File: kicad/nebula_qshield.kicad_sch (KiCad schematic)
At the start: 0 parts

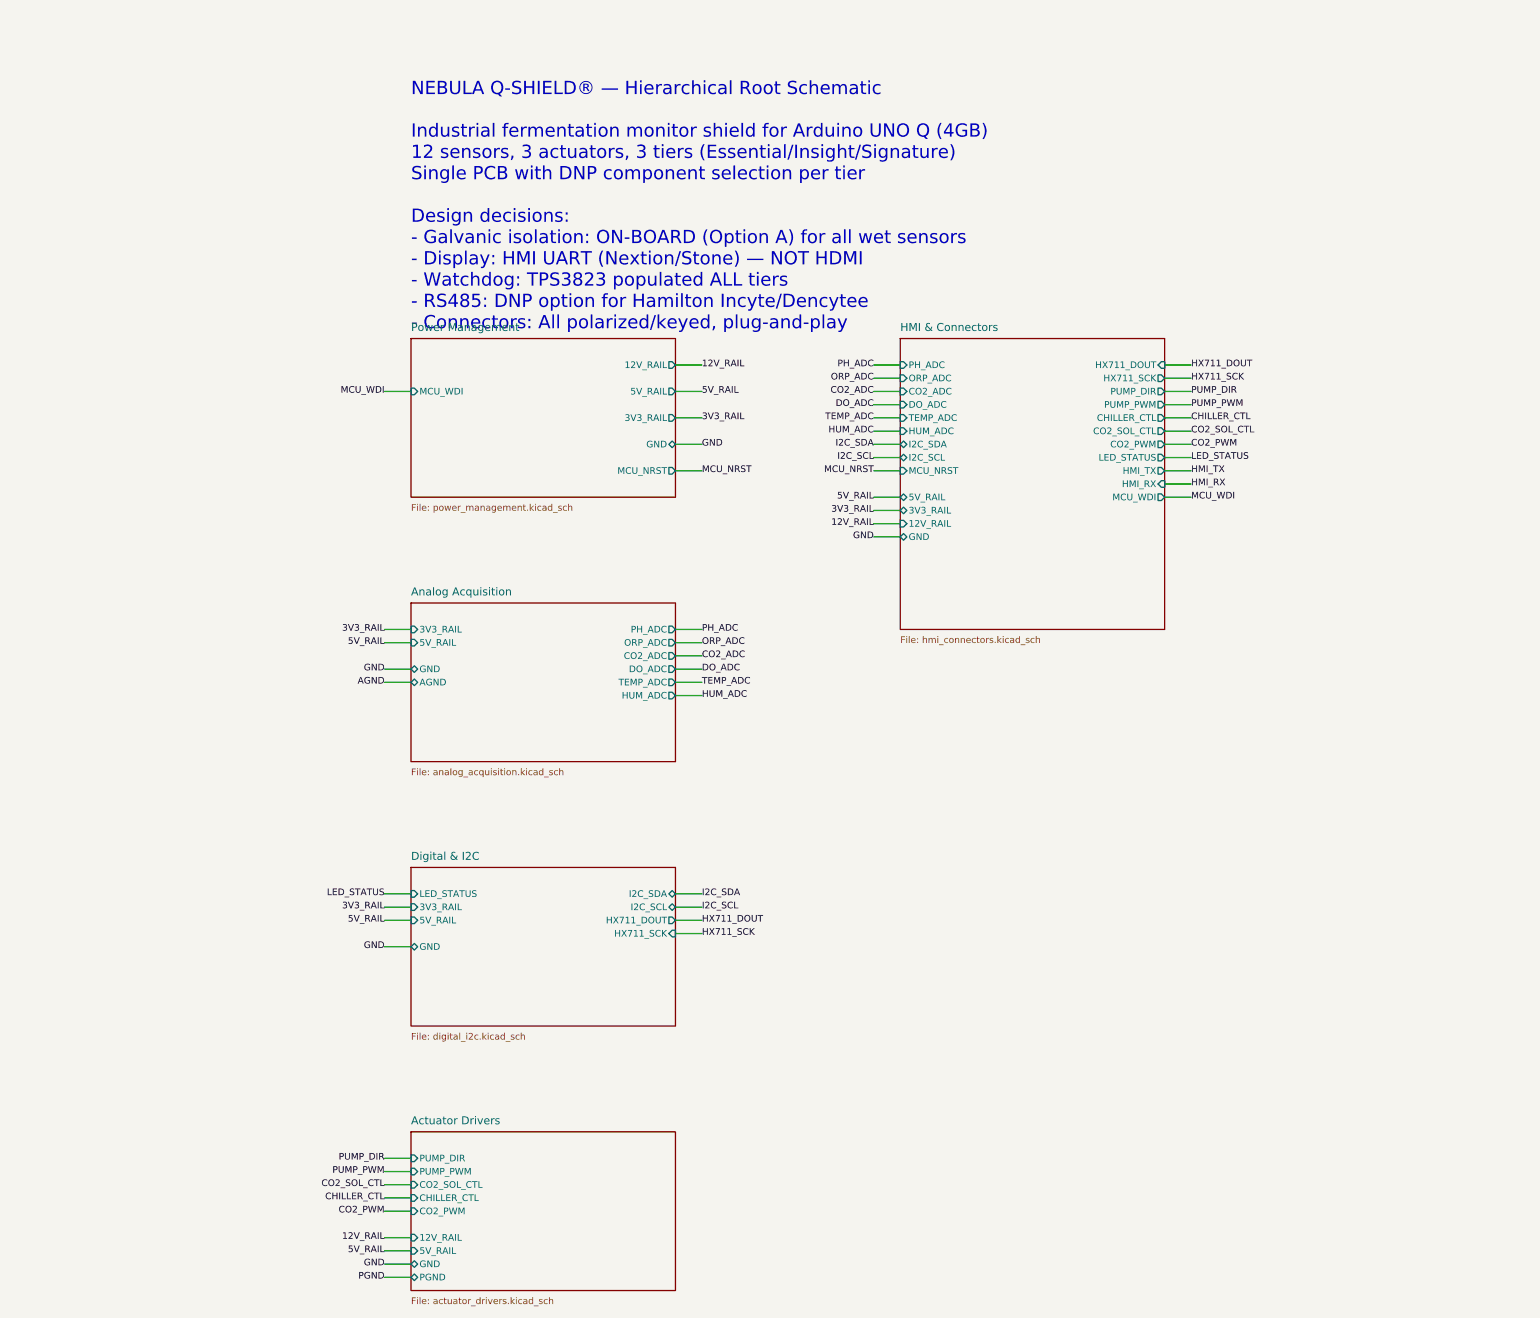
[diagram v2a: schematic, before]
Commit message: fix(grounding): unify AGND/PGND into GND, migrate CI to KiCad 10.0.5 — ERC 14→0
AGND and PGND were fully isolated nets with no path to GND, so the actuator
return path (MOSFET sources, opto emitters, gate-driver COM, flyback diodes,
terminal blocks) and the CO2/humidity sensor returns were floating. Merge them
into the single global GND net per the unified-grounding decision: one
continuous plane on layer 2, star grounding realised through placement and
local vias rather than split nets.

The isolated domains are untouched — GND_ISO_PH/ORP/DO (AMC1301 + SN6501
transformer) and GND_ISO (ISO1541) stay floating, since the galvanic barrier
lives in the isolators, not in a second ground plane.

- analog_acquisition: 2 AGND labels -> GND, legend stub removed
- actuator_drivers: 12 PGND labels -> GND, legend stub and its now-redundant
  PWR_FLAG removed
- hmi_connectors: HMI_TX/HMI_RX demoted from hierarchical to local labels; the
  UART is fully routed inside the sheet and nothing consumed the export
- root: 4 orphan sheet pins with their stub wires and labels removed
- CI container 9.0 -> 10.0.5, ERC severities pinned in the project file so the
  gate cannot weaken through a version bump, threshold 14 -> 0

Netlist verified pin-by-pin: 495 pins before and after, none lost or added,
exactly the 20 intended net reassignments. ERC clean under KiCad 10.0.5.

Co-Authored-By: Devin AI <158243242+devin-ai-integration[bot]@users.noreply.github.com>
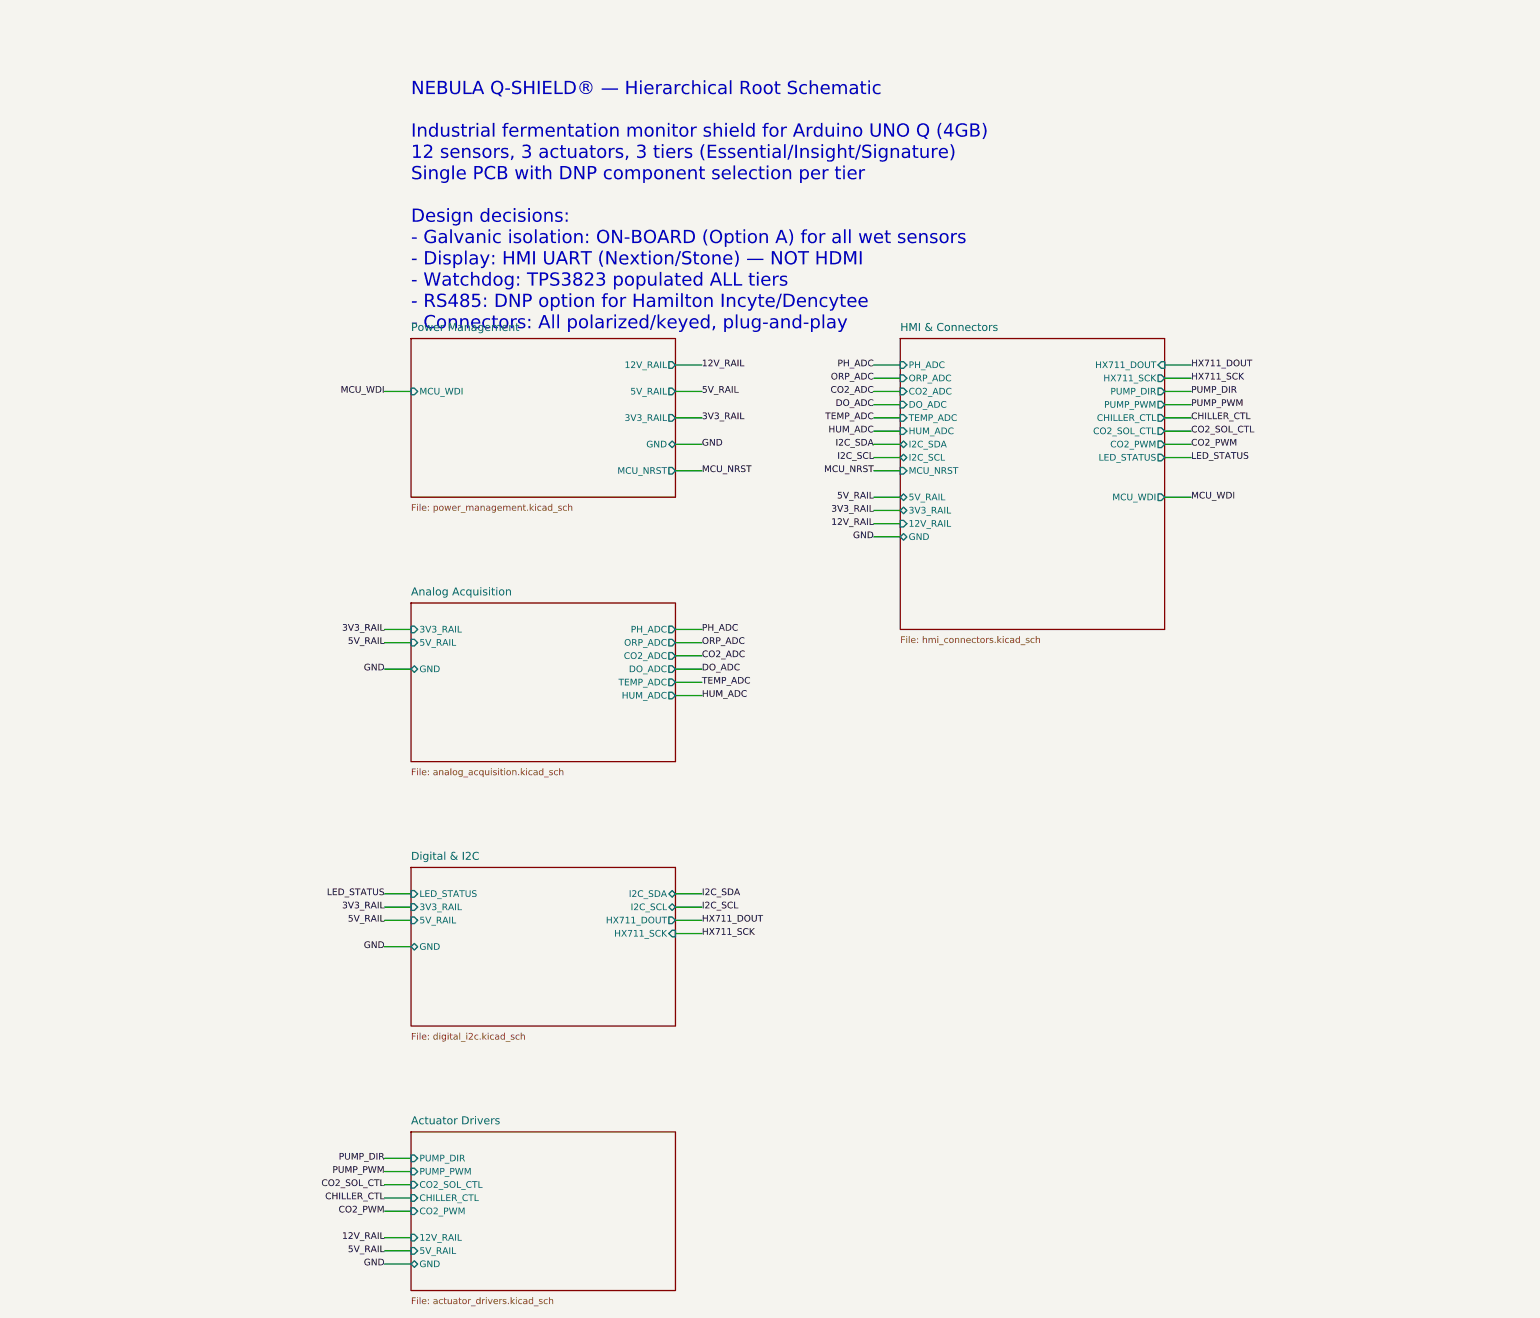
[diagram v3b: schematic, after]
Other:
- sheet Actuator Drivers ports: added none; removed PGND
- sheet Analog Acquisition ports: added none; removed AGND
- sheet HMI & Connectors ports: added none; removed HMI_RX, HMI_TX
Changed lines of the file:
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@@
     (pin "5V_RAIL"   input       (at 25.4 109.22 180)(effects (font (size 1.27 1.27))))
     (pin "GND"       bidirectional (at 25.4 114.3 180)(effects (font (size 1.27 1.27))))
-    (pin "AGND"      bidirectional (at 25.4 116.84 180)(effects (font (size 1.27 1.27))))
   )
   (sheet
@@
     (pin "5V_RAIL"     input   (at 25.4 226.06 180)  (effects (font (size 1.27 1.27))))
     (pin "GND"         bidirectional (at 25.4 228.6 180)(effects (font (size 1.27 1.27))))
-    (pin "PGND"        bidirectional (at 25.4 231.14 180)(effects (font (size 1.27 1.27))))
   )
   (sheet
@@
     (pin "CO2_PWM"     output      (at 170.18 71.12 0)    (effects (font (size 1.27 1.27))))
     (pin "LED_STATUS"  output      (at 170.18 73.66 0)    (effects (font (size 1.27 1.27))))
-    (pin "HMI_TX"      output      (at 170.18 76.2 0)     (effects (font (size 1.27 1.27))))
-    (pin "HMI_RX"      input       (at 170.18 78.74 0)    (effects (font (size 1.27 1.27))))
     (pin "MCU_WDI"     output      (at 170.18 81.28 0)    (effects (font (size 1.27 1.27))))
     (pin "MCU_NRST"    input       (at 119.38 76.2 180)   (effects (font (size 1.27 1.27))))
@@
   (wire (pts (xy 119.38 88.90) (xy 114.30 88.90)) (stroke (width 0) (type default)))
   (label "GND" (at 114.30 88.90 180) (effects (font (size 1.27 1.27))))
-  (wire (pts (xy 25.40 231.14) (xy 20.32 231.14)) (stroke (width 0) (type default)))
-  (label "PGND" (at 20.32 231.14 180) (effects (font (size 1.27 1.27))))
-  (wire (pts (xy 25.40 116.84) (xy 20.32 116.84)) (stroke (width 0) (type default)))
-  (label "AGND" (at 20.32 116.84 180) (effects (font (size 1.27 1.27))))
   (wire (pts (xy 76.20 106.68) (xy 81.28 106.68)) (stroke (width 0) (type default)))
   (label "PH_ADC" (at 81.28 106.68 0) (effects (font (size 1.27 1.27))))
@@
   (wire (pts (xy 119.38 76.20) (xy 114.30 76.20)) (stroke (width 0) (type default)))
   (label "MCU_NRST" (at 114.30 76.20 180) (effects (font (size 1.27 1.27))))
-  (wire (pts (xy 170.18 76.20) (xy 175.26 76.20)) (stroke (width 0) (type default)))
-  (label "HMI_TX" (at 175.26 76.20 0) (effects (font (size 1.27 1.27))))
-  (wire (pts (xy 170.18 78.74) (xy 175.26 78.74)) (stroke (width 0) (type default)))
-  (label "HMI_RX" (at 175.26 78.74 0) (effects (font (size 1.27 1.27))))
 )

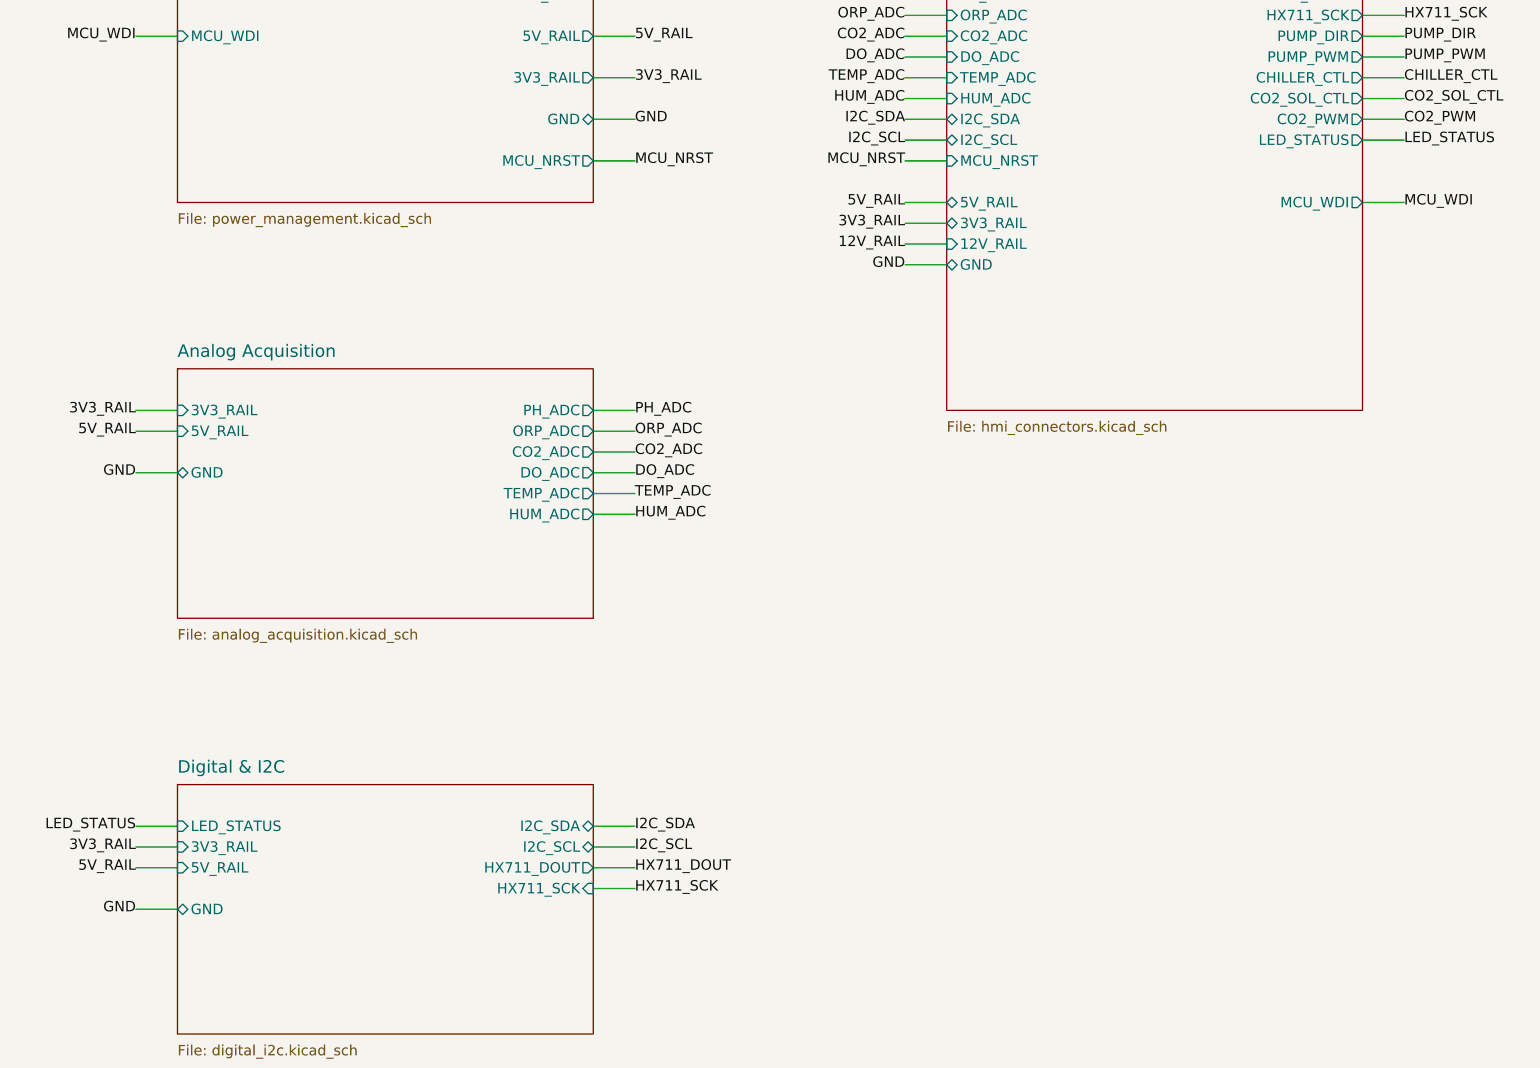
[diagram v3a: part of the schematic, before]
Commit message: feat(rs485): SC16IS740 I2C-UART bridge + realign J21 pin map to firmware
RS485 Modbus had no digital interface: U15's RO/~RE/DE/DI were carrying
no-connect flags, so ERC stayed silent while the transceiver was unusable.
The UNO Q has no free UART TX/RX pair (USART1 is the HMI, the alternate
pairs land on analog pins), so Modbus now hangs off the I2C bus through an
SC16IS740 bridge and coexists with the HMI.

- U22 SC16IS740 on I2C at 0x4D (A0/A1 low), Y1 1.8432 MHz + C31/C32,
  C33 decoupling, R38 pull-up on the open-drain ~IRQ, exported to J21 D10
- U23 SN74LVC1G04 inverts ~RTS into DE/~RE. The bridge leaves ~RTS high
  after POR, which would enable the driver and seize the multidrop bus
  before firmware runs; inverted it resets to driver-off/receive-on
- U15 MAX485ESA -> MAX3485CSA+ (same SOIC-8 pinout) because the bridge is
  not 5 V tolerant; digital_i2c no longer needs the 5 V rail
- J21 realigned to the firmware: D4=MCU_WDI, D6=PUMP_DIR, D8=CHILLER_CTL,
  D9=CO2_PWM. WDI previously shared D8 with the chiller relay, so driving
  the chiller would have kicked the watchdog

ERC 0 under KiCad 10.0.5; netlist diff limited to the intended pins.

Co-Authored-By: Devin AI <158243242+devin-ai-integration[bot]@users.noreply.github.com>
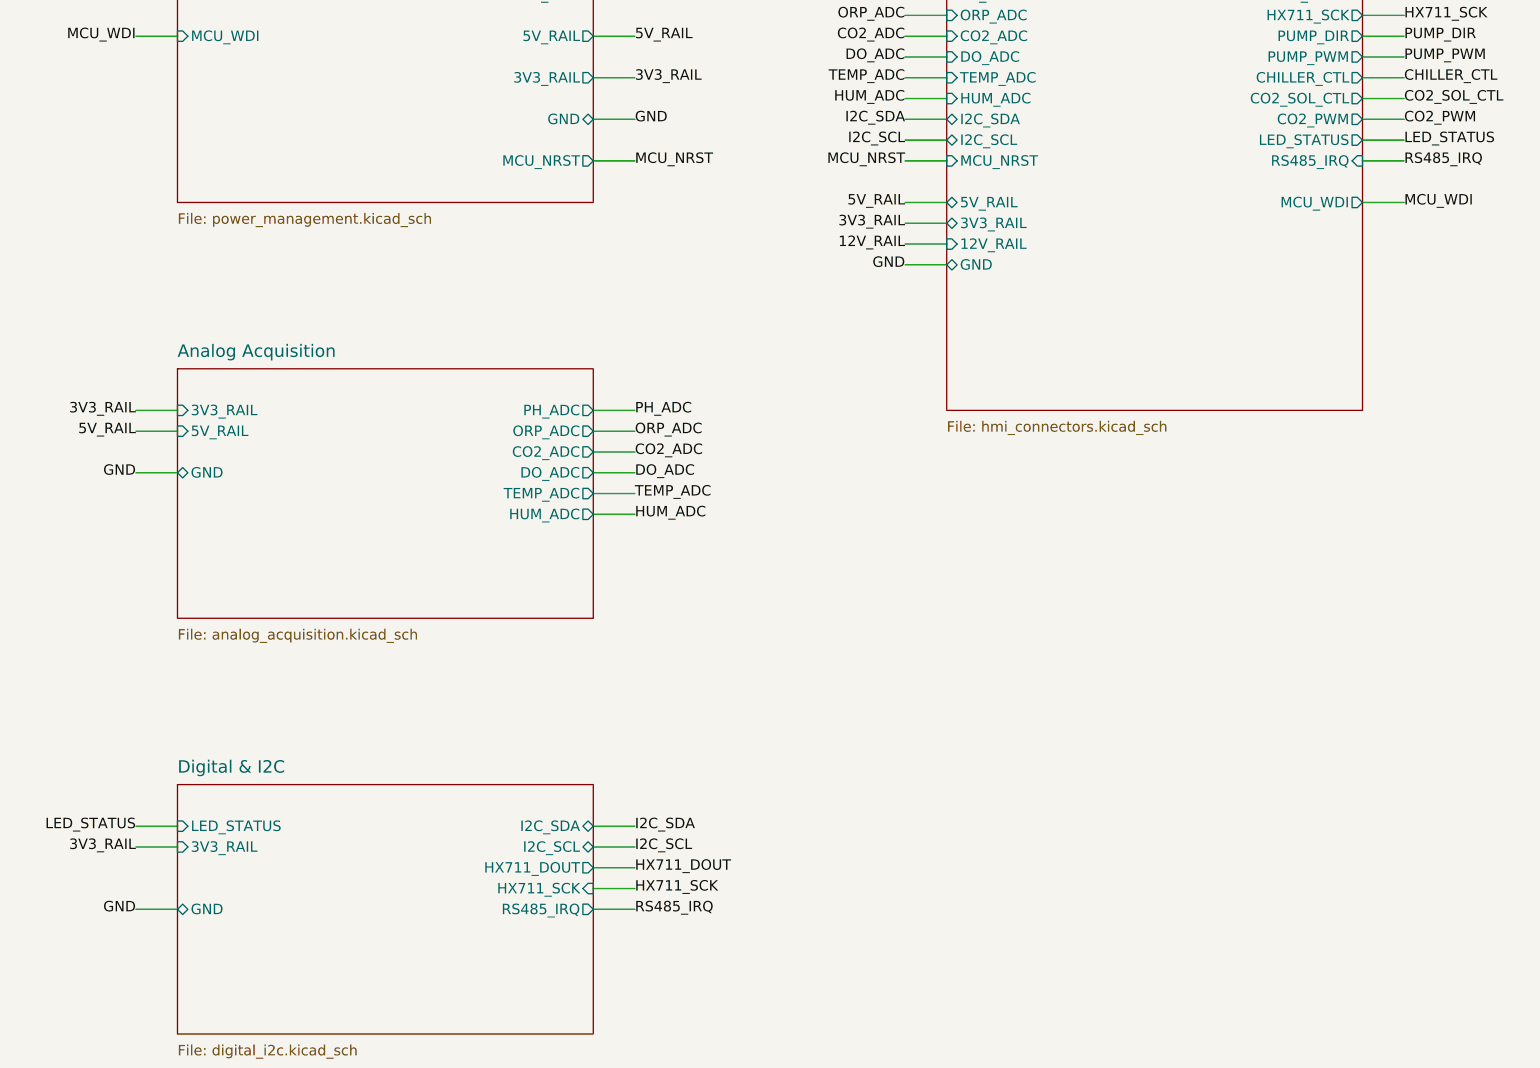
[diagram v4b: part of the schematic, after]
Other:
- sheet Digital & I2C ports: added RS485_IRQ; removed 5V_RAIL
- sheet HMI & Connectors ports: added RS485_IRQ; removed none
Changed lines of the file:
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@@
     (pin "LED_STATUS" input       (at 25.4 157.48 180)  (effects (font (size 1.27 1.27))))
     (pin "3V3_RAIL"   input       (at 25.4 160.02 180)  (effects (font (size 1.27 1.27))))
-    (pin "5V_RAIL"    input       (at 25.4 162.56 180)  (effects (font (size 1.27 1.27))))
     (pin "GND"        bidirectional (at 25.4 167.64 180)(effects (font (size 1.27 1.27))))
+      (pin "RS485_IRQ" output (at 76.20 167.64 0) (effects (font (size 1.27 1.27)) (justify left)))
   )
   (sheet
@@
     (pin "12V_RAIL"    input       (at 119.38 86.36 180)  (effects (font (size 1.27 1.27))))
     (pin "GND"         bidirectional (at 119.38 88.9 180) (effects (font (size 1.27 1.27))))
+      (pin "RS485_IRQ" input (at 170.18 76.20 0) (effects (font (size 1.27 1.27)) (justify left)))
   )
   (text "NEBULA Q-SHIELD® — Hierarchical Root Schematic\n\nIndustrial fermentation monitor shield for Arduino UNO Q (4GB)\n12 sensors, 3 actuators, 3 tiers (Essential/Insight/Signature)\nSingle PCB with DNP component selection per tier\n\nDesign decisions:\n- Galvanic isolation: ON-BOARD (Option A) for all wet sensors\n- Display: HMI UART (Nextion/Stone) — NOT HDMI\n- Watchdog: TPS3823 populated ALL tiers\n- RS485: DNP option for Hamilton Incyte/Dencytee\n- Connectors: All polarized/keyed, plug-and-play"
@@
   (wire (pts (xy 25.40 109.22) (xy 20.32 109.22)) (stroke (width 0) (type default)))
   (label "5V_RAIL" (at 20.32 109.22 180) (effects (font (size 1.27 1.27))))
-  (wire (pts (xy 25.40 162.56) (xy 20.32 162.56)) (stroke (width 0) (type default)))
-  (label "5V_RAIL" (at 20.32 162.56 180) (effects (font (size 1.27 1.27))))
   (wire (pts (xy 25.40 226.06) (xy 20.32 226.06)) (stroke (width 0) (type default)))
   (label "5V_RAIL" (at 20.32 226.06 180) (effects (font (size 1.27 1.27))))
@@
   (wire (pts (xy 119.38 76.20) (xy 114.30 76.20)) (stroke (width 0) (type default)))
   (label "MCU_NRST" (at 114.30 76.20 180) (effects (font (size 1.27 1.27))))
+  (wire (pts (xy 76.20 167.64) (xy 81.28 167.64)) (stroke (width 0) (type default)))
+  (label "RS485_IRQ" (at 81.28 167.64 0) (effects (font (size 1.27 1.27))))
+  (wire (pts (xy 170.18 76.20) (xy 175.26 76.20)) (stroke (width 0) (type default)))
+  (label "RS485_IRQ" (at 175.26 76.20 0) (effects (font (size 1.27 1.27))))
 )
